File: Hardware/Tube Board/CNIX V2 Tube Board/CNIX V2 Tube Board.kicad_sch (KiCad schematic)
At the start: 50 parts, among them J1 VDD, J2 GND, J3 Tube Conn, J4 LED, J5 HT, U1 SN75468, U10 IN-4_0, U11 IN-4_1, U12 IN-4_2, U13 IN-4_3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

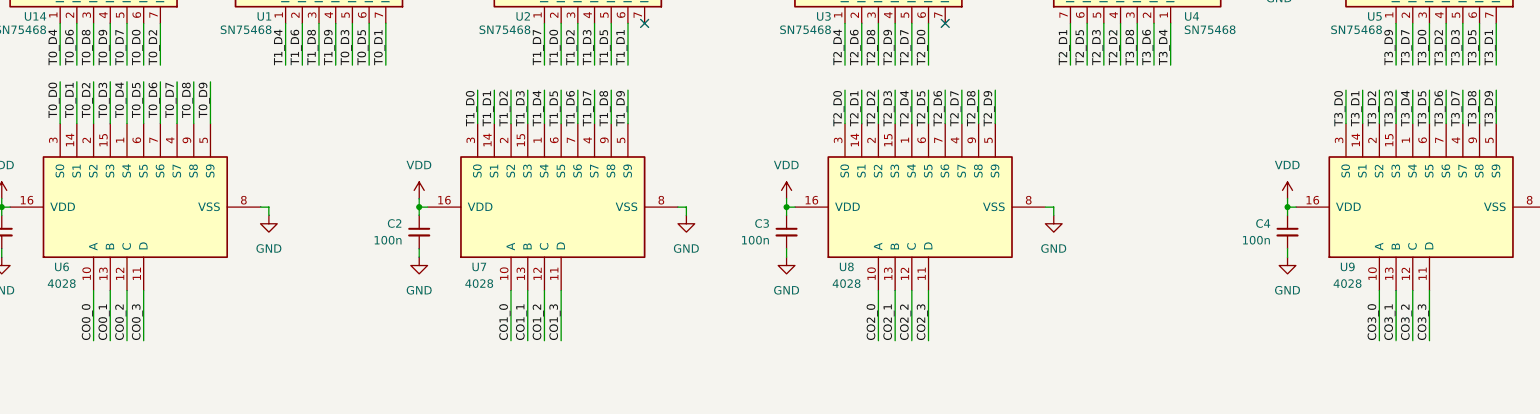
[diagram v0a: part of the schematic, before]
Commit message: added combined 3d model
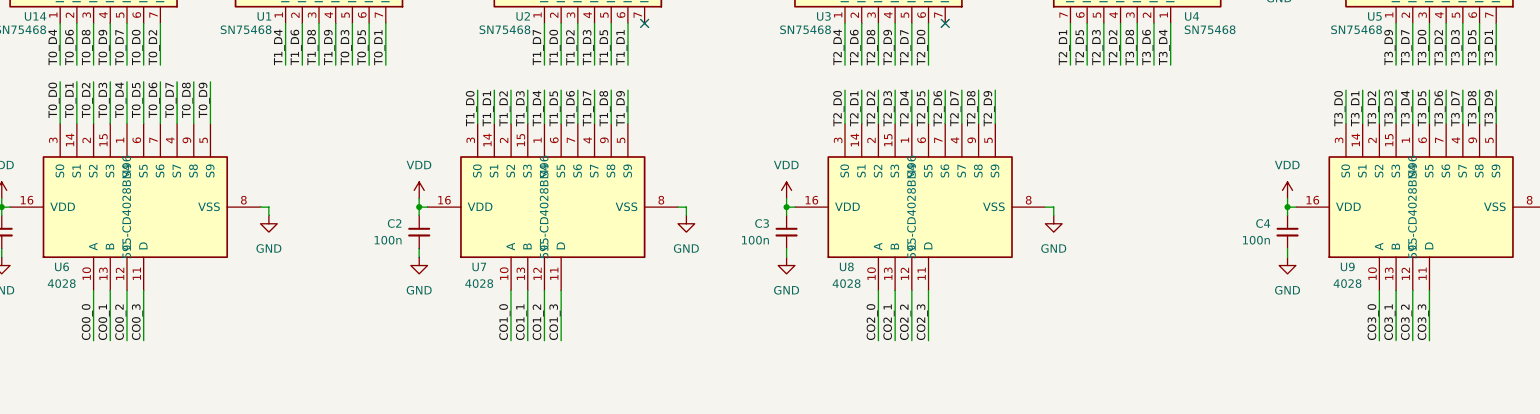
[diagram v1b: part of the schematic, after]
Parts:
- D1, D10, D13, D14, D2, D3, D4, D5, D6, D7, D8, D9: Mouser URL (none) -> 78-TZMC47
- R1, R12, R2, R3, R4, R5: Mouser Nr. (none) -> 603-AC0805FR-1347KL
- R10, R11: Mouser Nr. (none) -> 603-RC0805FR-074K7P
- R6, R7, R8, R9: Mouser Nr. (none) -> 603-RC1206FR-0718K7L
- U6, U7, U8, U9: Mouser Nr. (none) -> 595-CD4028BM96
